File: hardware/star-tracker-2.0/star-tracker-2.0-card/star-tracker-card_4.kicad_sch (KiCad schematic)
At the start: 18 parts, among them U1 RCLAMP0504FB, U7 OSD3358-512M-BSM, Y1 ECS-240-12-30BQ-AEN-TR, Y2 ABS07-32.768KHZ-T

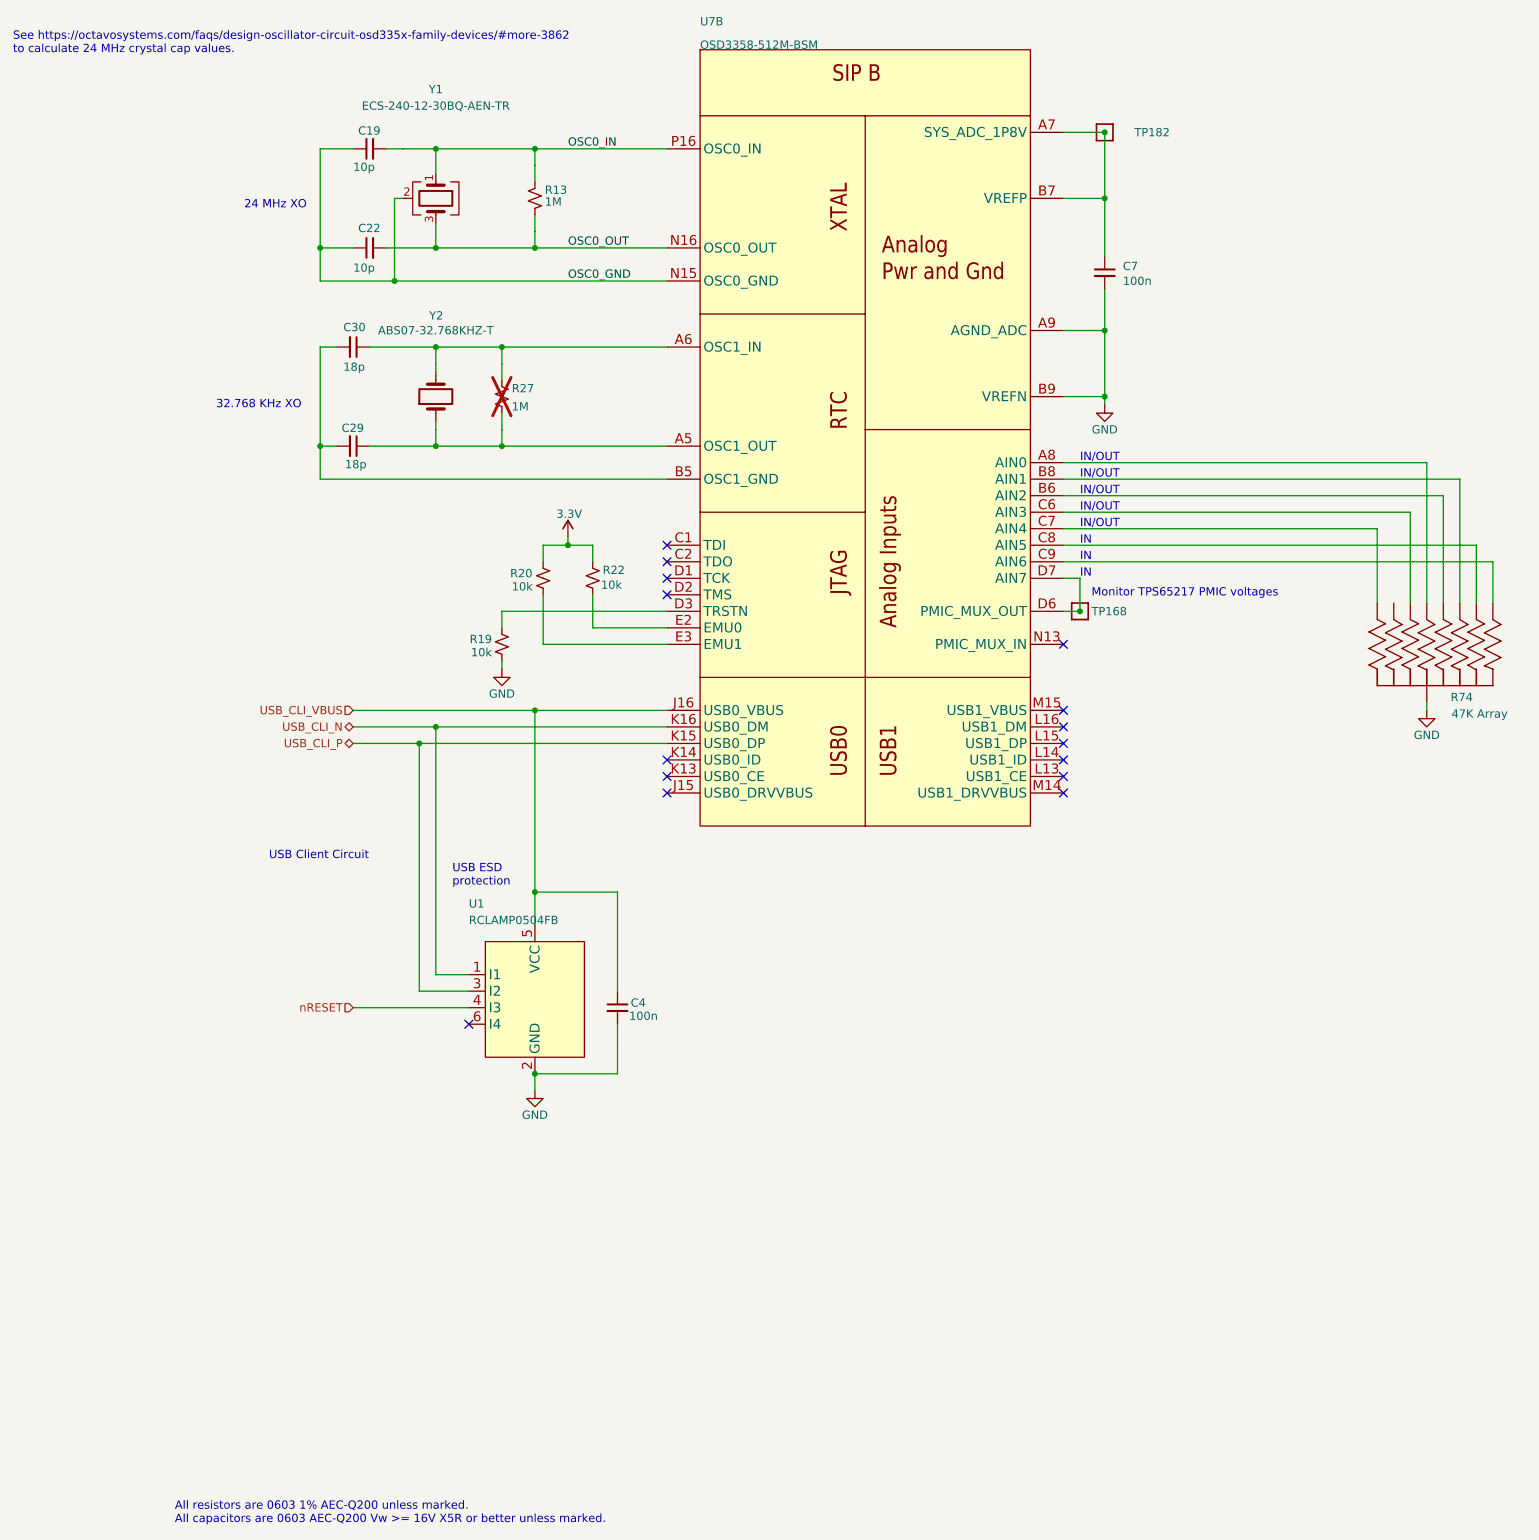
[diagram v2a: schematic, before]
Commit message: Star tracker board update
Added 3d models to footprints, reannotated component designators
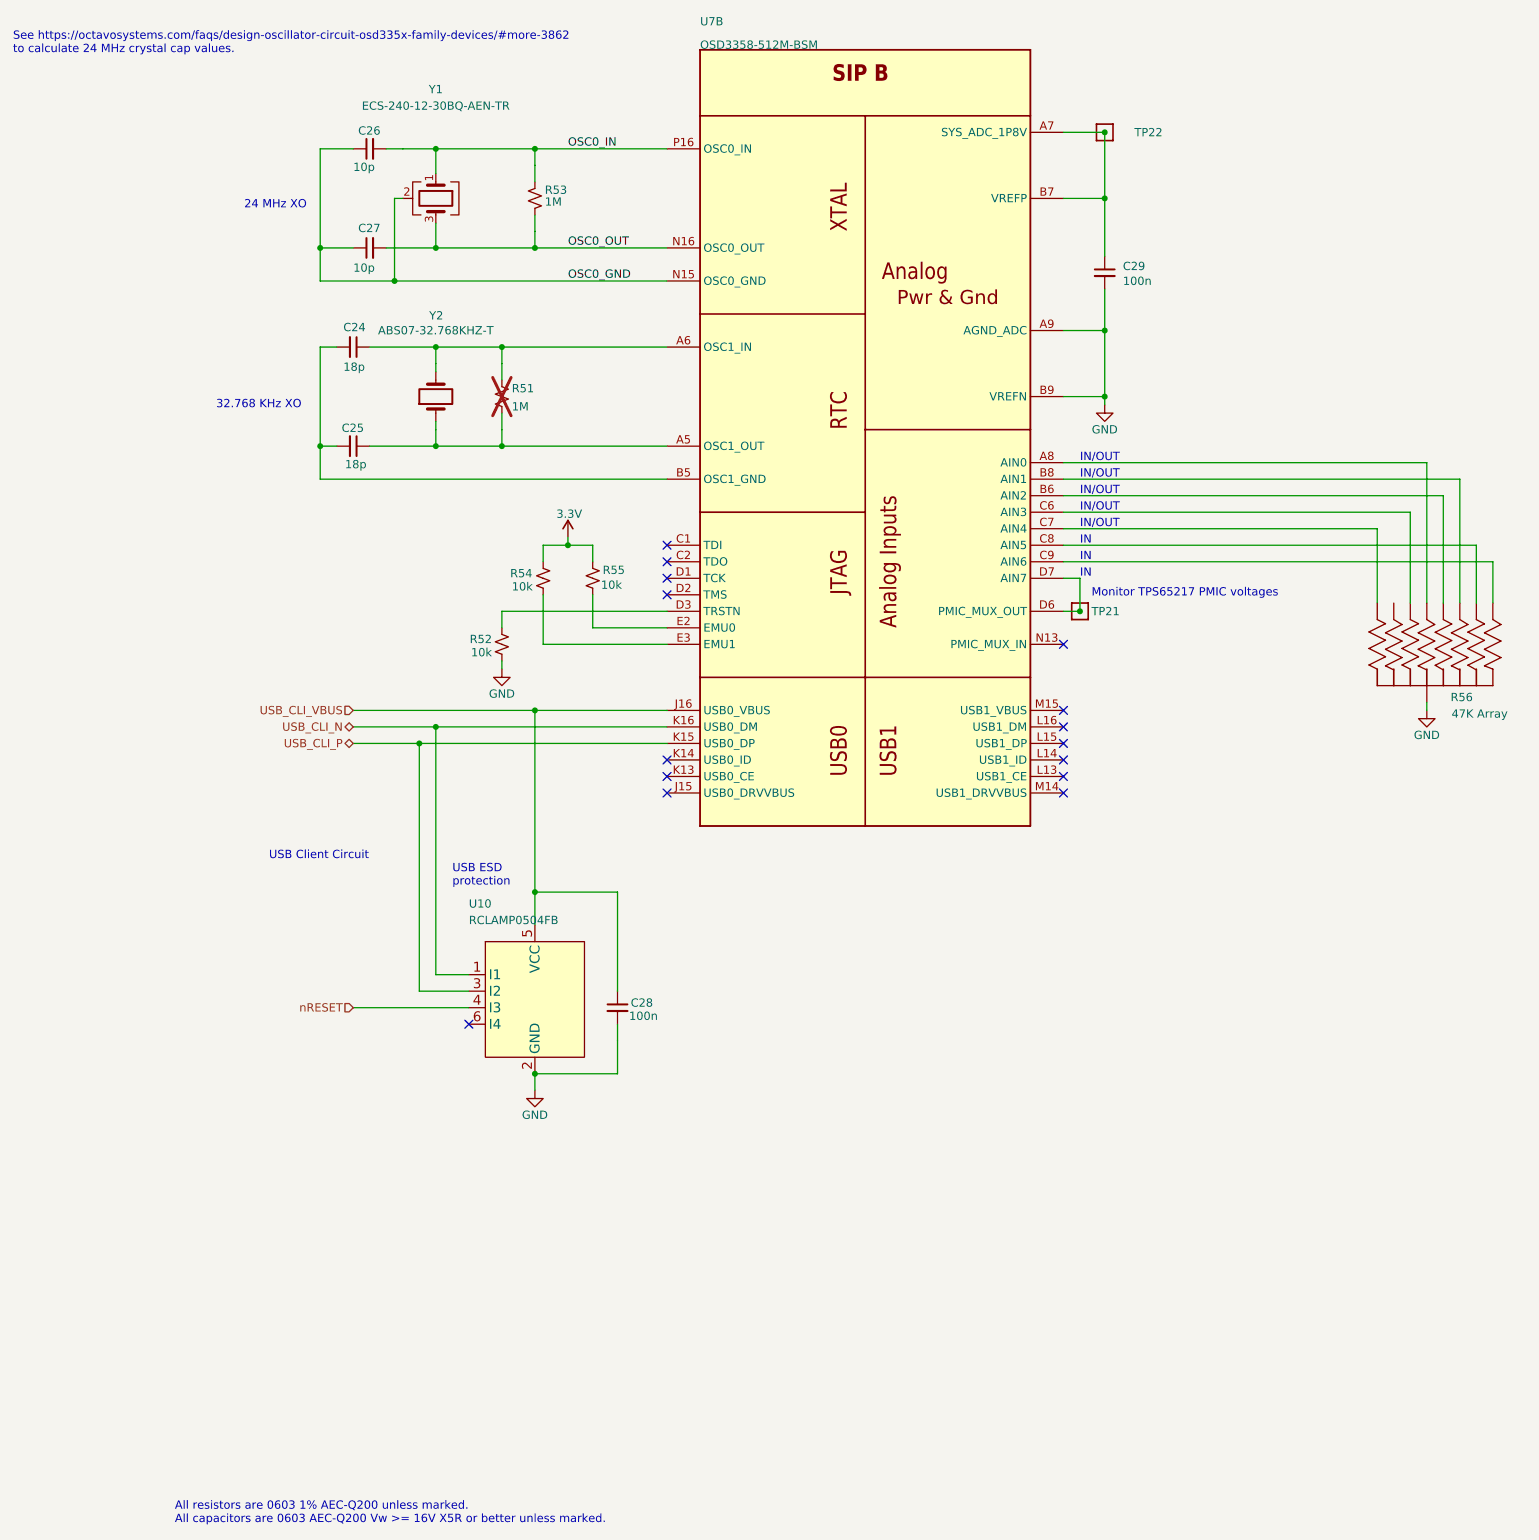
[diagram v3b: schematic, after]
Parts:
- U7: footprint star-tracker-card:OSD335X-BGA-256 -> oresat-ics:U-Octavo-OSD335X-BGA-256; symbol star-tracker-card-eagle-import:OSD3358-512M-BSM -> oresat-ics:OSD3358-512M-BSM; Distributor (none) -> DigiKey; MPN OSD3358-1G-ISM -> OSD3358-512M-BSM
- renumbered C30 to C24, C29 to C25, C19 to C26, C22 to C27, C4 to C28, C7 to C29, R27 to R51, R19 to R52, R13 to R53, R20 to R54, R22 to R55, R74 to R56, TP168 to TP21, TP182 to TP22, U1 to U10
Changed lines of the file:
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@@
 	(title_block
 		(title "OreSat Star Tracker")
-		(date "2026-04-22")
-		(rev "1.3")
+		(date "2026-06-05")
+		(rev "2.0")
 		(company "Portland State Aerospace Society")
 	)
@@
 		(in_pos_files yes)
 		(dnp no)
-		(property "Reference" "#PWR58"
+		(property "Reference" "#PWR047"
 			(at 162.56 139.7 0)
 			(hide yes)
@@
 			(project "star-tracker-card"
 				(path "/324e9eb5-7420-4b7e-862c-cc20bb28618a/180c7308-0a0c-41f6-9c76-108b10aa05c2"
-					(reference "#PWR58")
+					(reference "#PWR047")
 					(unit 1)
 				)
@@
 		(in_pos_files yes)
 		(dnp no)
-		(property "Reference" "TP168"
+		(property "Reference" "TP21"
 			(at 253.238 125.222 0)
 			(show_name no)
@@
 			(project "star-tracker-card"
 				(path "/324e9eb5-7420-4b7e-862c-cc20bb28618a/180c7308-0a0c-41f6-9c76-108b10aa05c2"
-					(reference "TP168")
+					(reference "TP21")
 					(unit 1)
 				)
@@
 		(in_pos_files yes)
 		(dnp no)
-		(property "Reference" "C4"
+		(property "Reference" "C28"
 			(at 182.372 185.42 0)
 			(show_name no)
@@
 			(project "star-tracker-card"
 				(path "/324e9eb5-7420-4b7e-862c-cc20bb28618a/180c7308-0a0c-41f6-9c76-108b10aa05c2"
-					(reference "C4")
+					(reference "C28")
 					(unit 1)
 				)
@@
 		(in_pos_files yes)
 		(dnp no)
-		(property "Reference" "TP182"
+		(property "Reference" "TP22"
 			(at 259.842 51.562 0)
 			(show_name no)
@@
 			(project "star-tracker-card"
 				(path "/324e9eb5-7420-4b7e-862c-cc20bb28618a/180c7308-0a0c-41f6-9c76-108b10aa05c2"
-					(reference "TP182")
+					(reference "TP22")
 					(unit 1)
 				)
@@
 		(in_pos_files yes)
 		(dnp no)
-		(property "Reference" "R13"
+		(property "Reference" "R53"
 			(at 169.164 58.928 0)
 			(show_name no)
@@
 			(project "star-tracker-card"
 				(path "/324e9eb5-7420-4b7e-862c-cc20bb28618a/180c7308-0a0c-41f6-9c76-108b10aa05c2"
-					(reference "R13")
+					(reference "R53")
 					(unit 1)
 				)
@@
 		(in_pos_files yes)
 		(dnp no)
-		(property "Reference" "R74"
+		(property "Reference" "R56"
 			(at 308.4576 138.43 90)
 			(show_name no)
@@
 			(project "star-tracker-card"
 				(path "/324e9eb5-7420-4b7e-862c-cc20bb28618a/180c7308-0a0c-41f6-9c76-108b10aa05c2"
-					(reference "R74")
+					(reference "R56")
 					(unit 1)
 				)
@@
 		(in_pos_files yes)
 		(dnp no)
-		(property "Reference" "R22"
+		(property "Reference" "R55"
 			(at 178.054 118.872 0)
 			(show_name no)
@@
 			(project "star-tracker-card"
 				(path "/324e9eb5-7420-4b7e-862c-cc20bb28618a/180c7308-0a0c-41f6-9c76-108b10aa05c2"
-					(reference "R22")
+					(reference "R55")
 					(unit 1)
 				)
@@
 		(in_pos_files yes)
 		(dnp no)
-		(property "Reference" "R19"
+		(property "Reference" "R52"
 			(at 161.036 128.016 0)
 			(show_name no)
@@
 			(project "star-tracker-card"
 				(path "/324e9eb5-7420-4b7e-862c-cc20bb28618a/180c7308-0a0c-41f6-9c76-108b10aa05c2"
-					(reference "R19")
+					(reference "R52")
 					(unit 1)
 				)
@@
 		(in_pos_files yes)
 		(dnp no)
-		(property "Reference" "C22"
+		(property "Reference" "C27"
 			(at 140.462 66.294 90)
 			(show_name no)
@@
 			(project "star-tracker-card"
 				(path "/324e9eb5-7420-4b7e-862c-cc20bb28618a/180c7308-0a0c-41f6-9c76-108b10aa05c2"
-					(reference "C22")
+					(reference "C27")
 					(unit 1)
 				)
@@
 		(in_pos_files yes)
 		(dnp no)
-		(property "Reference" "C19"
+		(property "Reference" "C26"
 			(at 140.462 51.308 90)
 			(show_name no)
@@
 			(project "star-tracker-card"
 				(path "/324e9eb5-7420-4b7e-862c-cc20bb28618a/180c7308-0a0c-41f6-9c76-108b10aa05c2"
-					(reference "C19")
+					(reference "C26")
 					(unit 1)
 				)
@@
 		(in_pos_files yes)
 		(dnp no)
-		(property "Reference" "#PWR35"
+		(property "Reference" "#PWR049"
 			(at 255.27 99.06 0)
 			(hide yes)
@@
 			(project "star-tracker-card"
 				(path "/324e9eb5-7420-4b7e-862c-cc20bb28618a/180c7308-0a0c-41f6-9c76-108b10aa05c2"
-					(reference "#PWR35")
+					(reference "#PWR049")
 					(unit 1)
 				)
@@
 		(in_pos_files yes)
 		(dnp no)
-		(property "Reference" "C30"
+		(property "Reference" "C24"
 			(at 138.176 81.534 90)
 			(show_name no)
@@
 			(project "star-tracker-card"
 				(path "/324e9eb5-7420-4b7e-862c-cc20bb28618a/180c7308-0a0c-41f6-9c76-108b10aa05c2"
-					(reference "C30")
+					(reference "C24")
 					(unit 1)
 				)
@@
 		(in_pos_files yes)
 		(dnp no)
-		(property "Reference" "#PWR59"
+		(property "Reference" "#PWR048"
 			(at 167.64 204.47 0)
 			(hide yes)
@@
 			(project "star-tracker-card"
 				(path "/324e9eb5-7420-4b7e-862c-cc20bb28618a/180c7308-0a0c-41f6-9c76-108b10aa05c2"
-					(reference "#PWR59")
+					(reference "#PWR048")
 					(unit 1)
 				)
@@
 		(in_pos_files yes)
 		(dnp no)
-		(property "Reference" "#3V-024"
+		(property "Reference" "#3V-06"
 			(at 172.72 110.49 0)
 			(hide yes)
@@
 			(project "star-tracker-card"
 				(path "/324e9eb5-7420-4b7e-862c-cc20bb28618a/180c7308-0a0c-41f6-9c76-108b10aa05c2"
-					(reference "#3V-024")
+					(reference "#3V-06")
 					(unit 1)
 				)
@@
 		(in_pos_files yes)
 		(dnp yes)
-		(property "Reference" "R27"
+		(property "Reference" "R51"
 			(at 164.084 90.932 0)
 			(show_name no)
@@
 			(project "star-tracker-card"
 				(path "/324e9eb5-7420-4b7e-862c-cc20bb28618a/180c7308-0a0c-41f6-9c76-108b10aa05c2"
-					(reference "R27")
+					(reference "R51")
 					(unit 1)
 				)
@@
 		(in_pos_files yes)
 		(dnp no)
-		(property "Reference" "U1"
+		(property "Reference" "U10"
 			(at 157.48 170.18 0)
 			(show_name no)
@@
 			(project "star-tracker-card"
 				(path "/324e9eb5-7420-4b7e-862c-cc20bb28618a/180c7308-0a0c-41f6-9c76-108b10aa05c2"
-					(reference "U1")
+					(reference "U10")
 					(unit 1)
 				)
@@
 		(in_pos_files yes)
 		(dnp no)
-		(property "Reference" "R20"
+		(property "Reference" "R54"
 			(at 163.83 119.38 0)
 			(show_name no)
@@
 			(project "star-tracker-card"
 				(path "/324e9eb5-7420-4b7e-862c-cc20bb28618a/180c7308-0a0c-41f6-9c76-108b10aa05c2"
-					(reference "R20")
+					(reference "R54")
 					(unit 1)
 				)
@@
 		(in_pos_files yes)
 		(dnp no)
-		(property "Reference" "C29"
+		(property "Reference" "C25"
 			(at 137.922 97.028 90)
 			(show_name no)
@@
 			(project "star-tracker-card"
 				(path "/324e9eb5-7420-4b7e-862c-cc20bb28618a/180c7308-0a0c-41f6-9c76-108b10aa05c2"
-					(reference "C29")
+					(reference "C25")
 					(unit 1)
 				)
@@
 		(in_pos_files yes)
 		(dnp no)
-		(property "Reference" "#PWR5"
+		(property "Reference" "#PWR050"
 			(at 304.8 146.05 0)
 			(hide yes)
@@
 			(project "star-tracker-card"
 				(path "/324e9eb5-7420-4b7e-862c-cc20bb28618a/180c7308-0a0c-41f6-9c76-108b10aa05c2"
-					(reference "#PWR5")
+					(reference "#PWR050")
 					(unit 1)
 				)
@@
 		(in_pos_files yes)
 		(dnp no)
-		(property "Reference" "C7"
+		(property "Reference" "C29"
 			(at 258.064 72.136 0)
 			(show_name no)
@@
 			(project "star-tracker-card"
 				(path "/324e9eb5-7420-4b7e-862c-cc20bb28618a/180c7308-0a0c-41f6-9c76-108b10aa05c2"
-					(reference "C7")
+					(reference "C29")
 					(unit 1)
 				)
@@
 	)
 	(symbol
-		(lib_id "star-tracker-card-eagle-import:OSD3358-512M-BSM")
+		(lib_id "oresat-ics:OSD3358-512M-BSM")
 		(at 218.44 96.52 0)
 		(unit 2)
@@
 			)
 		)
-		(property "Footprint" "star-tracker-card:OSD335X-BGA-256"
-			(at 218.44 96.52 0)
+		(property "Footprint" "oresat-ics:U-Octavo-OSD335X-BGA-256"
+			(at 218.44 -11.43 0)
 			(hide yes)
 			(show_name no)
@@
 			)
 		)
-		(property "Description" "OSD335x Embedded Module ARM® Cortex®-A8, AM3358 1GHz 1GB"
-			(at 218.44 96.52 0)
+		(property "Description" "OSD335x Embedded Module 1GHz 512MB"
+			(at 218.44 -7.62 0)
 			(hide yes)
 			(show_name no)
@@
 			)
 		)
-		(property "MPN" "OSD3358-1G-ISM"
-			(at 218.44 96.52 0)
+		(property "MPN" "OSD3358-512M-BSM"
+			(at 218.44 -2.54 0)
+			(hide yes)
+			(show_name no)
+			(do_not_autoplace no)
+			(effects
+				(font
+					(size 1.27 1.27)
+				)
+			)
+		)
+		(property "Distributor" "DigiKey"
+			(at 218.44 -5.08 0)
 			(hide yes)
 			(show_name no)

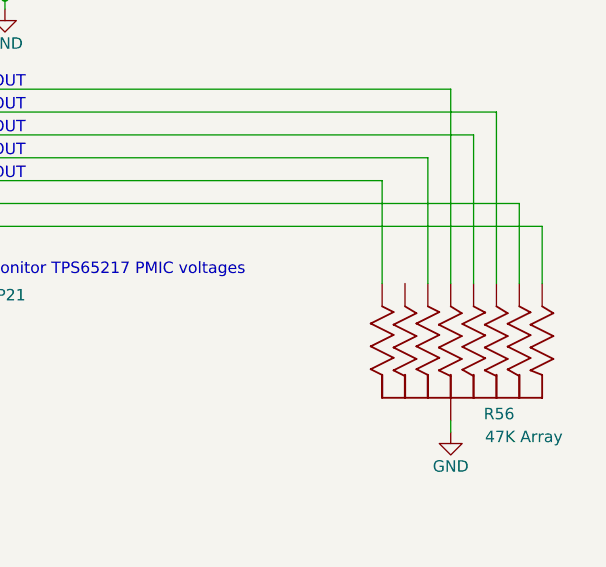
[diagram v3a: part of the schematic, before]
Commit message: Bom update
Updated BOM to correct connector MPN and other misc components
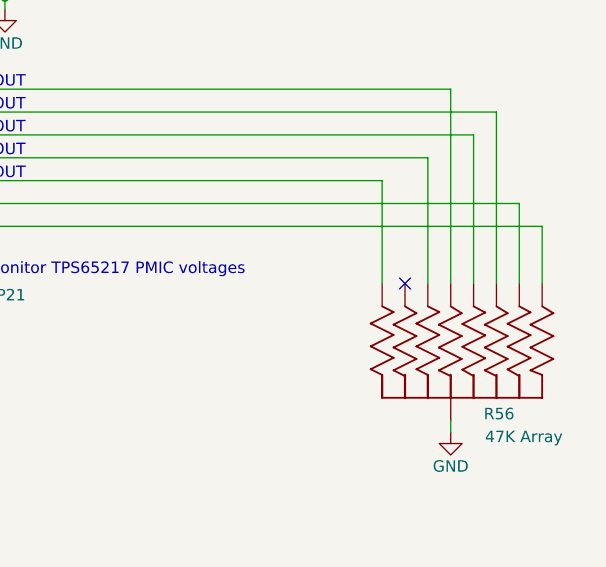
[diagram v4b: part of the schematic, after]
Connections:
- no-connect marks 15 -> 16
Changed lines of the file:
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@@
+	)
+	(no_connect
+		(at 299.72 123.19)
 	)
 	(no_connect
